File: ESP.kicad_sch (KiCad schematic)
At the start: 22 parts, among them J1 Conn_01x04_Pin, J2 Conn_01x02_Pin, SW1 SW_Push, U1 ESP32-WROVER-E-N4R8, U7 TPS56339DDCR

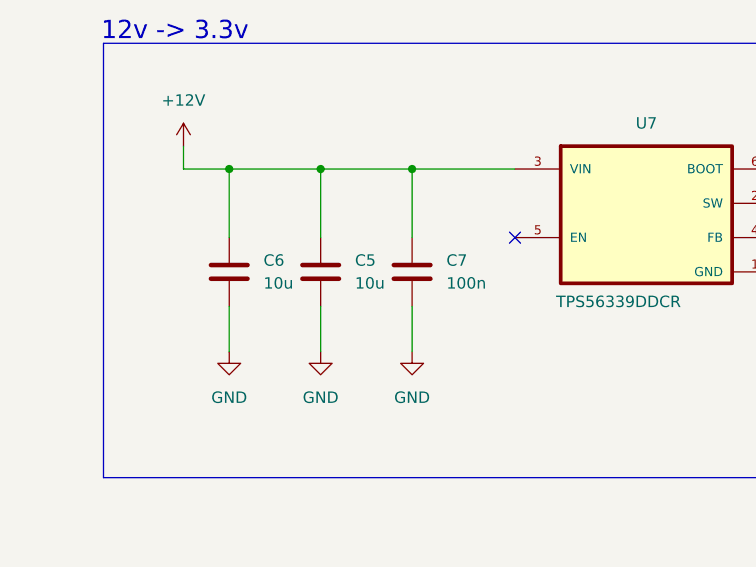
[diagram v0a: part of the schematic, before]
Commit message: fix: specify 25V rating on caps on the 12V rail (#3)
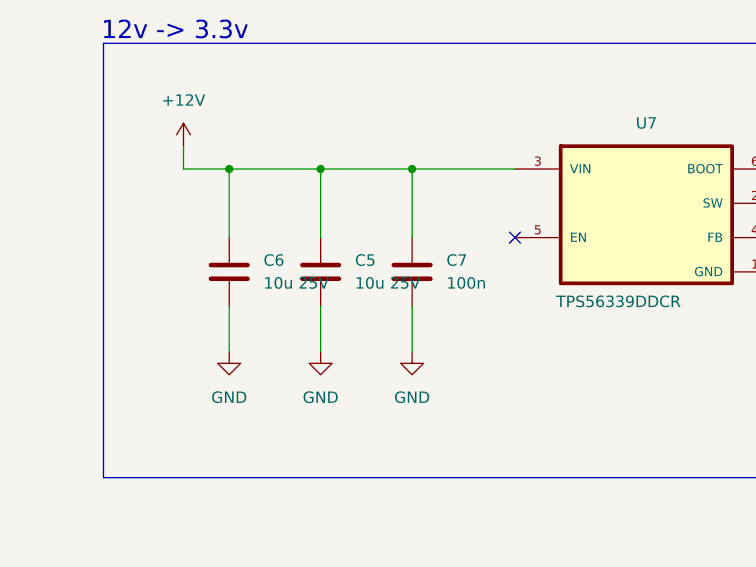
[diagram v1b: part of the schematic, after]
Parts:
- C5, C6: value 10u -> 10u 25V
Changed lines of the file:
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@@
 			)
 		)
-		(property "Value" "10u"
+		(property "Value" "10u 25V"
 			(at 45.72 44.4499 0)
 			(effects
@@
 			)
 		)
-		(property "Value" "10u"
+		(property "Value" "10u 25V"
 			(at 55.88 44.4499 0)
 			(effects
